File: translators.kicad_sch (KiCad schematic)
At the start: 53 parts, among them U10 SN74AXC8T245_UQFN, U2 SN74AXC8T245_UQFN, U3 SN74AXC8T245_UQFN, U4 SN74AXC8T245_UQFN, U5 SN74AXC8T245_UQFN, U6 SN74AXC8T245_UQFN

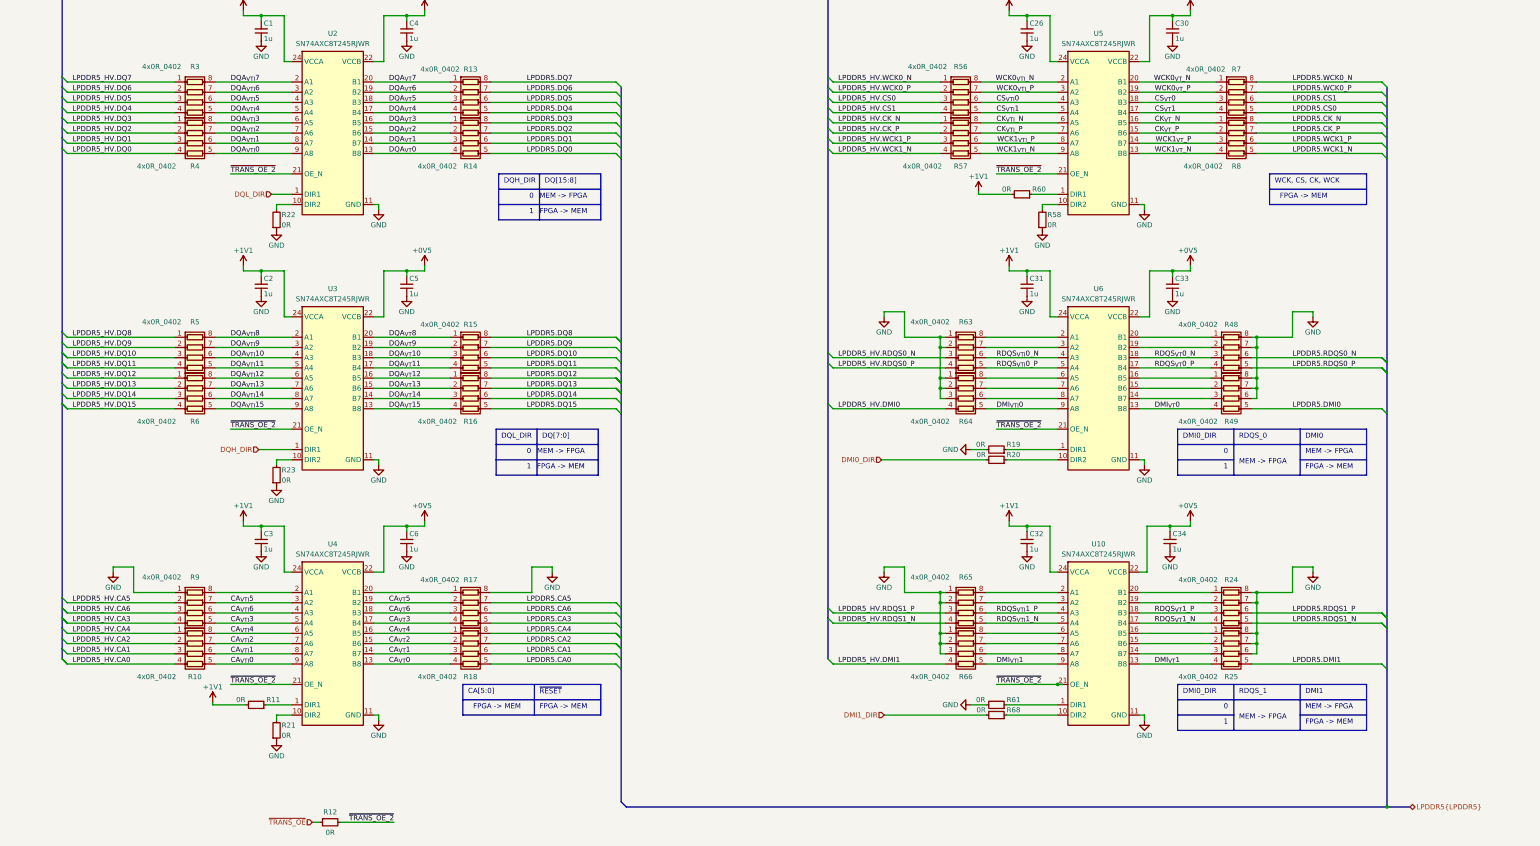
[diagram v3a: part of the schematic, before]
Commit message: [#52835] schematics: update translators pinout to for better package breakout
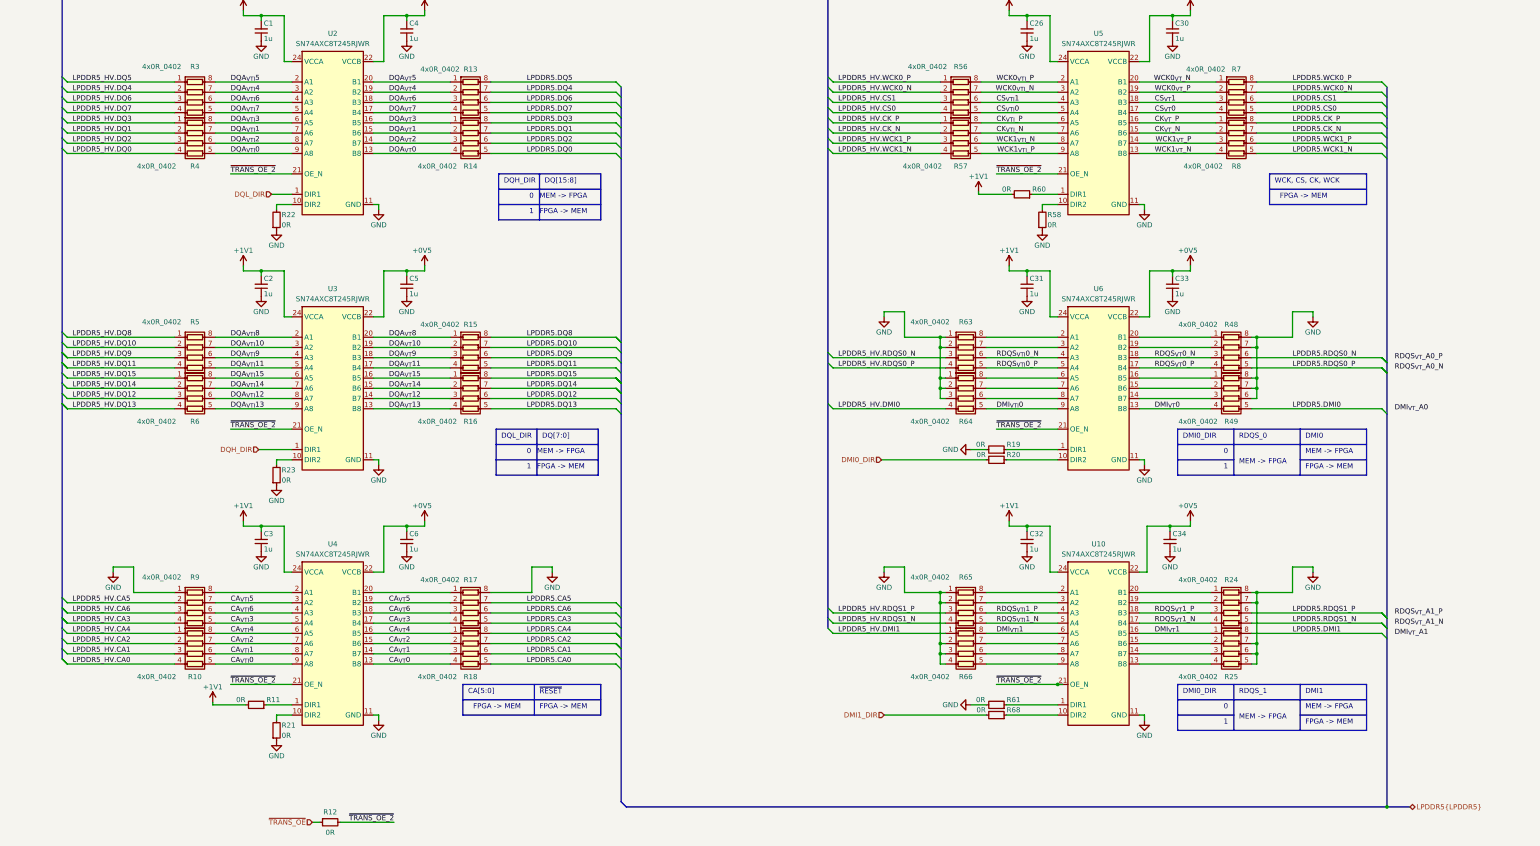
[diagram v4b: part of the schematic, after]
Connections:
- net CK_{VTI}_N: now also R57.7 (R2.2), U5.7 (A6); no longer R57.8 (R1.2), U5.6 (A5)
- net CK_{VTI}_P: now also R57.8 (R1.2), U5.6 (A5); no longer R57.7 (R2.2), U5.7 (A6)
- net CK_{VT}_N: now also R8.2 (R2.1), U5.15 (B6); no longer R8.1 (R1.1), U5.16 (B5)
- net CK_{VT}_P: now also R8.1 (R1.1), U5.16 (B5); no longer R8.2 (R2.1), U5.15 (B6)
- net CS_{VTI}0: now also R56.5 (R4.2), U5.5 (A4); no longer R56.6 (R3.2), U5.4 (A3)
- net CS_{VTI}1: now also R56.6 (R3.2), U5.4 (A3); no longer R56.5 (R4.2), U5.5 (A4)
- net CS_{VT}0: now also R7.4 (R4.1), U5.17 (B4); no longer R7.3 (R3.1), U5.18 (B3)
- net CS_{VT}1: now also R7.3 (R3.1), U5.18 (B3); no longer R7.4 (R4.1), U5.17 (B4)
- net DMI_{VTI}1: now also R66.8 (R1.2), U10.6 (A5); no longer R66.5 (R4.2), U10.9 (A8)
- net DMI_{VT}1: now also R25.1 (R1.1), U10.16 (B5); no longer R25.4 (R4.1), U10.13 (B8)
- net DQA_{VTI}1: now also R4.7 (R2.2), U2.7 (A6); no longer R4.6 (R3.2), U2.8 (A7)
- net DQA_{VTI}10: now also R5.7 (R2.2), U3.3 (A2); no longer R5.6 (R3.2), U3.4 (A3)
- net DQA_{VTI}12: now also R6.6 (R3.2), U3.8 (A7); no longer R6.8 (R1.2), U3.6 (A5)
- net DQA_{VTI}13: now also R6.5 (R4.2), U3.9 (A8); no longer R6.7 (R2.2), U3.7 (A6)
- net DQA_{VTI}14: now also R6.7 (R2.2), U3.7 (A6); no longer R6.6 (R3.2), U3.8 (A7)
- net DQA_{VTI}15: now also R6.8 (R1.2), U3.6 (A5); no longer R6.5 (R4.2), U3.9 (A8)
- net DQA_{VTI}2: now also R4.6 (R3.2), U2.8 (A7); no longer R4.7 (R2.2), U2.7 (A6)
- net DQA_{VTI}4: now also R3.7 (R2.2), U2.3 (A2); no longer R3.5 (R4.2), U2.5 (A4)
- net DQA_{VTI}5: now also R3.8 (R1.2), U2.2 (A1); no longer R3.6 (R3.2), U2.4 (A3)
- net DQA_{VTI}6: now also R3.6 (R3.2), U2.4 (A3); no longer R3.7 (R2.2), U2.3 (A2)
- net DQA_{VTI}7: now also R3.5 (R4.2), U2.5 (A4); no longer R3.8 (R1.2), U2.2 (A1)
- net DQA_{VTI}9: now also R5.6 (R3.2), U3.4 (A3); no longer R5.7 (R2.2), U3.3 (A2)
- net DQA_{VT}1: now also R14.2 (R2.1), U2.15 (B6); no longer R14.3 (R3.1), U2.14 (B7)
- net DQA_{VT}10: now also R15.2 (R2.1), U3.19 (B2); no longer R15.3 (R3.1), U3.18 (B3)
- net DQA_{VT}12: now also R16.3 (R3.1), U3.14 (B7); no longer R16.1 (R1.1), U3.16 (B5)
- net DQA_{VT}13: now also R16.4 (R4.1), U3.13 (B8); no longer R16.2 (R2.1), U3.15 (B6)
- net DQA_{VT}14: now also R16.2 (R2.1), U3.15 (B6); no longer R16.3 (R3.1), U3.14 (B7)
- net DQA_{VT}15: now also R16.1 (R1.1), U3.16 (B5); no longer R16.4 (R4.1), U3.13 (B8)
- net DQA_{VT}2: now also R14.3 (R3.1), U2.14 (B7); no longer R14.2 (R2.1), U2.15 (B6)
- net DQA_{VT}4: now also R13.2 (R2.1), U2.19 (B2); no longer R13.4 (R4.1), U2.17 (B4)
- net DQA_{VT}5: now also R13.1 (R1.1), U2.20 (B1); no longer R13.3 (R3.1), U2.18 (B3)
- net DQA_{VT}6: now also R13.3 (R3.1), U2.18 (B3); no longer R13.2 (R2.1), U2.19 (B2)
- net DQA_{VT}7: now also R13.4 (R4.1), U2.17 (B4); no longer R13.1 (R1.1), U2.20 (B1)
- net DQA_{VT}9: now also R15.3 (R3.1), U3.18 (B3); no longer R15.2 (R2.1), U3.19 (B2)
- net GND: now also R25.5 (R4.2), R66.4 (R4.1); no longer R25.8 (R1.2), R66.1 (R1.1)
- net LPDDR5.CK_N: now also R8.7 (R2.2); no longer R8.8 (R1.2)
- net LPDDR5.CK_P: now also R8.8 (R1.2); no longer R8.7 (R2.2)
- net LPDDR5.DMI1: now also R25.8 (R1.2); no longer R25.5 (R4.2)
- net LPDDR5.DQ1: now also R14.7 (R2.2); no longer R14.6 (R3.2)
- net LPDDR5.DQ10: now also R15.7 (R2.2); no longer R15.6 (R3.2)
- net LPDDR5.DQ12: now also R16.6 (R3.2); no longer R16.8 (R1.2)
- net LPDDR5.DQ13: now also R16.5 (R4.2); no longer R16.7 (R2.2)
- net LPDDR5.DQ14: now also R16.7 (R2.2); no longer R16.6 (R3.2)
- net LPDDR5.DQ15: now also R16.8 (R1.2); no longer R16.5 (R4.2)
- net LPDDR5.DQ2: now also R14.6 (R3.2); no longer R14.7 (R2.2)
- net LPDDR5.DQ4: now also R13.7 (R2.2); no longer R13.5 (R4.2)
- net LPDDR5.DQ5: now also R13.8 (R1.2); no longer R13.6 (R3.2)
- net LPDDR5.DQ6: now also R13.6 (R3.2); no longer R13.7 (R2.2)
- net LPDDR5.DQ7: now also R13.5 (R4.2); no longer R13.8 (R1.2)
- net LPDDR5.DQ9: now also R15.6 (R3.2); no longer R15.7 (R2.2)
- net LPDDR5.WCK0_N: now also R7.7 (R2.2); no longer R7.8 (R1.2)
- net LPDDR5.WCK0_P: now also R7.8 (R1.2); no longer R7.7 (R2.2)
- net LPDDR5_HV.CK_N: now also R57.2 (R2.1); no longer R57.1 (R1.1)
- net LPDDR5_HV.CK_P: now also R57.1 (R1.1); no longer R57.2 (R2.1)
- net LPDDR5_HV.CS0: now also R56.4 (R4.1); no longer R56.3 (R3.1)
- net LPDDR5_HV.CS1: now also R56.3 (R3.1); no longer R56.4 (R4.1)
- net LPDDR5_HV.DMI1: now also R66.1 (R1.1); no longer R66.4 (R4.1)
- net LPDDR5_HV.DQ1: now also R4.2 (R2.1); no longer R4.3 (R3.1)
- net LPDDR5_HV.DQ10: now also R5.2 (R2.1); no longer R5.3 (R3.1)
- net LPDDR5_HV.DQ12: now also R6.3 (R3.1); no longer R6.1 (R1.1)
- net LPDDR5_HV.DQ13: now also R6.4 (R4.1); no longer R6.2 (R2.1)
- net LPDDR5_HV.DQ14: now also R6.2 (R2.1); no longer R6.3 (R3.1)
- net LPDDR5_HV.DQ15: now also R6.1 (R1.1); no longer R6.4 (R4.1)
- net LPDDR5_HV.DQ2: now also R4.3 (R3.1); no longer R4.2 (R2.1)
- net LPDDR5_HV.DQ4: now also R3.2 (R2.1); no longer R3.4 (R4.1)
- net LPDDR5_HV.DQ5: now also R3.1 (R1.1); no longer R3.3 (R3.1)
- net LPDDR5_HV.DQ6: now also R3.3 (R3.1); no longer R3.2 (R2.1)
- net LPDDR5_HV.DQ7: now also R3.4 (R4.1); no longer R3.1 (R1.1)
- net LPDDR5_HV.DQ9: now also R5.3 (R3.1); no longer R5.2 (R2.1)
- net LPDDR5_HV.WCK0_N: now also R56.2 (R2.1); no longer R56.1 (R1.1)
- net LPDDR5_HV.WCK0_P: now also R56.1 (R1.1); no longer R56.2 (R2.1)
- net WCK0_{VTI}_N: now also R56.7 (R2.2), U5.3 (A2); no longer R56.8 (R1.2), U5.2 (A1)
- net WCK0_{VTI}_P: now also R56.8 (R1.2), U5.2 (A1); no longer R56.7 (R2.2), U5.3 (A2)
- net WCK1_{VTI}_N: now also R57.6 (R3.2), U5.8 (A7); no longer R57.5 (R4.2), U5.9 (A8)
- net WCK1_{VTI}_P: now also R57.5 (R4.2), U5.9 (A8); no longer R57.6 (R3.2), U5.8 (A7)
- new net: R25.4 (R4.1), U10.13 (B8)
- new net: R66.5 (R4.2), U10.9 (A8)

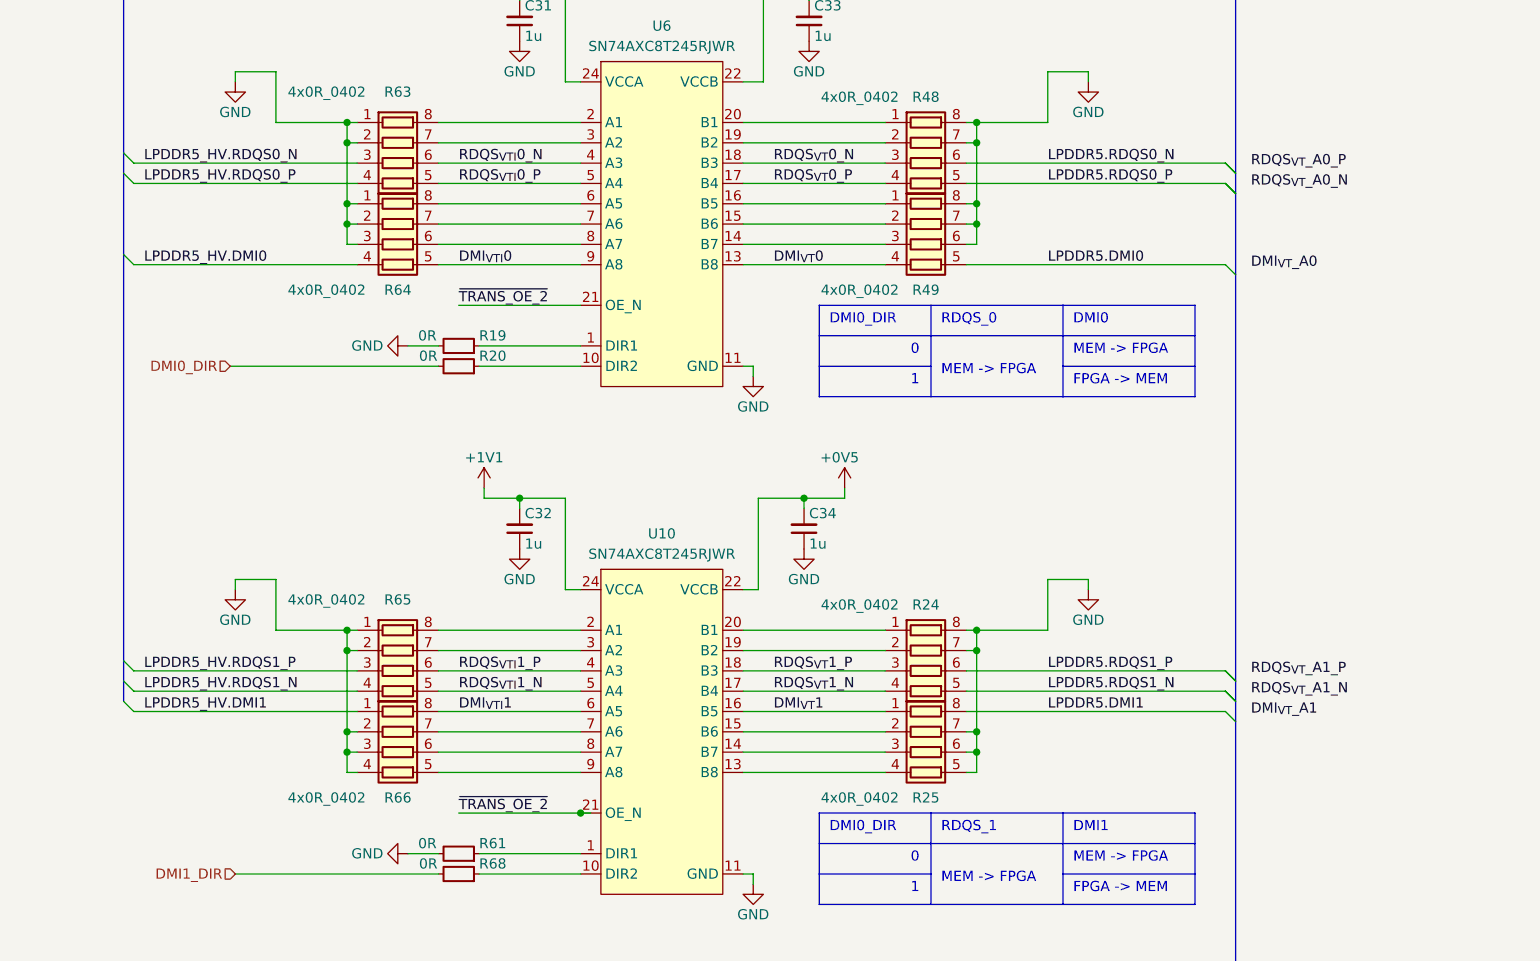
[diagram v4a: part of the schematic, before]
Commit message: [#52536] schematics: add additional decoupling to DDR die
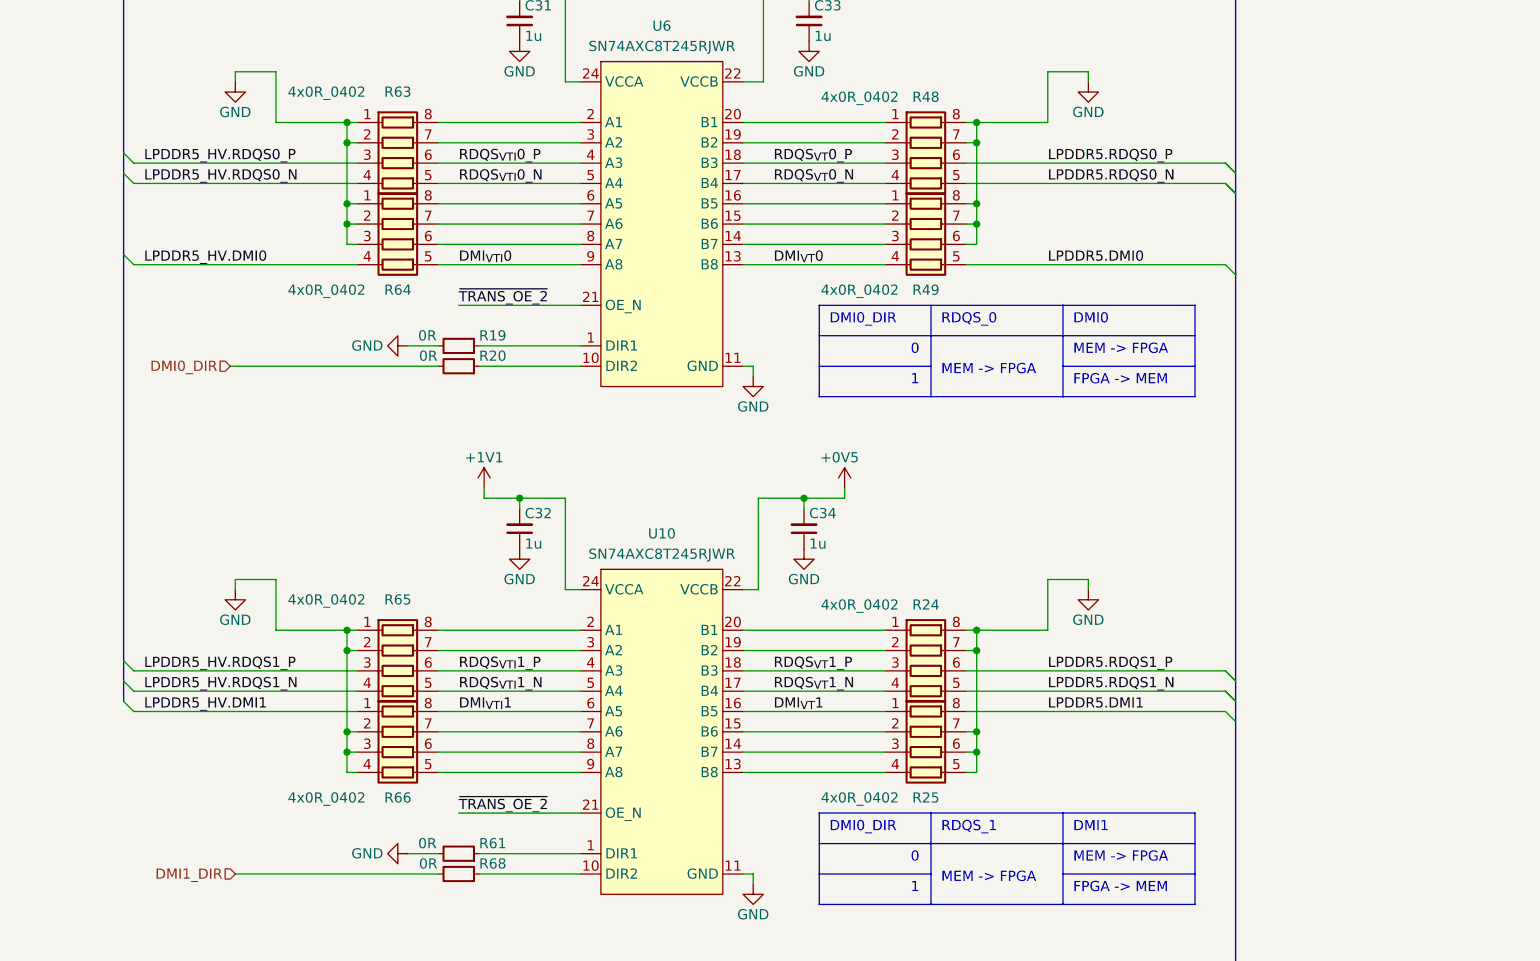
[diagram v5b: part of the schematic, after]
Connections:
- net LPDDR5.RDQS0_N: now also R48.5 (R4.2); no longer R48.6 (R3.2)
- net LPDDR5.RDQS0_P: now also R48.6 (R3.2); no longer R48.5 (R4.2)
- net LPDDR5_HV.RDQS0_N: now also R63.4 (R4.1); no longer R63.3 (R3.1)
- net LPDDR5_HV.RDQS0_P: now also R63.3 (R3.1); no longer R63.4 (R4.1)
- net RDQS_{VTI}0_N: now also R63.5 (R4.2), U6.5 (A4); no longer R63.6 (R3.2), U6.4 (A3)
- net RDQS_{VTI}0_P: now also R63.6 (R3.2), U6.4 (A3); no longer R63.5 (R4.2), U6.5 (A4)
- net RDQS_{VT}0_N: now also R48.4 (R4.1), U6.17 (B4); no longer R48.3 (R3.1), U6.18 (B3)
- net RDQS_{VT}0_P: now also R48.3 (R3.1), U6.18 (B3); no longer R48.4 (R4.1), U6.17 (B4)
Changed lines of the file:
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@@
   (junction (at 266.7 186.69) (diameter 0) (color 0 0 0 0)
   )
-  (junction (at 295.91 207.01) (diameter 0) (color 0 0 0 0)
-  )
   (junction (at 345.44 184.15) (diameter 0) (color 0 0 0 0)
   )
@@
     (stroke (width 0) (type default) (color 0 0 0 0))
   )
-  (wire (pts (xy 295.91 207.01) (xy 297.18 207.01))
-    (stroke (width 0) (type default) (color 0 0 0 0))
-  )
   (wire (pts (xy 344.17 186.69) (xy 345.44 186.69))
     (stroke (width 0) (type default) (color 0 0 0 0))
@@
     (effects (font (size 1.27 1.27)) (justify left bottom))
   )
-  (label "RDQS_{VT}_A0_P" (at 379.73 126.365 0)
-    (effects (font (size 1.27 1.27)) (justify left bottom))
-  )
   (label "LPDDR5.RDQS1_P" (at 354.33 189.23 0)
     (effects (font (size 1.27 1.27)) (justify left bottom))
@@
     (effects (font (size 1.27 1.27)) (justify left bottom))
   )
-  (label "LPDDR5.RDQS0_P" (at 354.33 128.27 0)
+  (label "LPDDR5.RDQS0_P" (at 354.33 125.73 0)
     (effects (font (size 1.27 1.27)) (justify left bottom))
   )
-  (label "RDQS_{VTI}0_N" (at 280.67 125.73 0)
+  (label "RDQS_{VTI}0_N" (at 280.67 128.27 0)
     (effects (font (size 1.27 1.27)) (justify left bottom))
   )
@@
     (effects (font (size 1.27 1.27)) (justify left bottom))
   )
-  (label "DMI_{VT}_A0" (at 379.73 139.065 0)
-    (effects (font (size 1.27 1.27)) (justify left bottom))
-  )
   (label "DQA_{VT}11" (at 129.54 128.27 0)
     (effects (font (size 1.27 1.27)) (justify left bottom))
@@
     (effects (font (size 1.27 1.27)) (justify left bottom))
   )
-  (label "LPDDR5.RDQS0_N" (at 354.33 125.73 0)
+  (label "LPDDR5.RDQS0_N" (at 354.33 128.27 0)
     (effects (font (size 1.27 1.27)) (justify left bottom))
   )
@@
     (effects (font (size 1.27 1.27)) (justify left bottom))
   )
-  (label "RDQS_{VT}_A1_P" (at 379.73 189.865 0)
-    (effects (font (size 1.27 1.27)) (justify left bottom))
-  )
   (label "LPDDR5.RDQS1_N" (at 354.33 191.77 0)
     (effects (font (size 1.27 1.27)) (justify left bottom))
@@
     (effects (font (size 1.27 1.27)) (justify left bottom))
   )
-  (label "RDQS_{VTI}0_P" (at 280.67 128.27 0)
+  (label "RDQS_{VTI}0_P" (at 280.67 125.73 0)
     (effects (font (size 1.27 1.27)) (justify left bottom))
   )
@@
     (effects (font (size 1.27 1.27)) (justify left bottom))
   )
-  (label "RDQS_{VT}_A1_N" (at 379.73 192.405 0)
-    (effects (font (size 1.27 1.27)) (justify left bottom))
-  )
   (label "LPDDR5_HV.DQ12" (at 50.8 135.89 0)
     (effects (font (size 1.27 1.27)) (justify left bottom))
@@
     (effects (font (size 1.27 1.27)) (justify left bottom))
   )
-  (label "RDQS_{VT}0_P" (at 320.04 128.27 0)
+  (label "RDQS_{VT}0_P" (at 320.04 125.73 0)
     (effects (font (size 1.27 1.27)) (justify left bottom))
   )
@@
     (effects (font (size 1.27 1.27)) (justify left bottom))
   )
-  (label "RDQS_{VT}_A0_N" (at 379.73 128.905 0)
-    (effects (font (size 1.27 1.27)) (justify left bottom))
-  )
   (label "LPDDR5.WCK0_P" (at 354.33 57.15 0)
     (effects (font (size 1.27 1.27)) (justify left bottom))
@@
     (effects (font (size 1.27 1.27)) (justify left bottom))
   )
-  (label "LPDDR5_HV.RDQS0_P" (at 241.3 128.27 0)
+  (label "LPDDR5_HV.RDQS0_P" (at 241.3 125.73 0)
     (effects (font (size 1.27 1.27)) (justify left bottom))
   )
@@
     (effects (font (size 1.27 1.27)) (justify left bottom))
   )
-  (label "DMI_{VT}_A1" (at 379.73 194.945 0)
-    (effects (font (size 1.27 1.27)) (justify left bottom))
-  )
   (label "~{TRANS_OE_2}" (at 130.81 241.3 180)
     (effects (font (size 1.27 1.27)) (justify right bottom))
@@
     (effects (font (size 1.27 1.27)) (justify left bottom))
   )
-  (label "LPDDR5_HV.RDQS0_N" (at 241.3 125.73 0)
+  (label "LPDDR5_HV.RDQS0_N" (at 241.3 128.27 0)
     (effects (font (size 1.27 1.27)) (justify left bottom))
   )
@@
     (effects (font (size 1.27 1.27)) (justify left bottom))
   )
-  (label "RDQS_{VT}0_N" (at 320.04 125.73 0)
+  (label "RDQS_{VT}0_N" (at 320.04 128.27 0)
     (effects (font (size 1.27 1.27)) (justify left bottom))
   )
